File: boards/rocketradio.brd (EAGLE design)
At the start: 103.8 x 82.5 mm, 28 parts, among them T1 2N2222, X1 BU-SMA-H

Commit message: finish dumb node, update sims
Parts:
- removed C10: 0.1uF, rcl:C0603
- removed R10, R11, R12, R8, R9: (no value), rcl:R0603
- removed U$10: CSTCE16M0V53-R0, evan:MYSMD2_RESONATOR
- removed U$2, U$3: ATTINY85SOCKET, evan:SOCKET-08
- added BATT+, BATT-, COM, JP1, JP3, NC, NO: (no value), evan:1X01
- added K1: G5LE, relay:G5LE
- added MICRO, MODEM: ATTINY85SOCKET, evan:SOCKET-08
- C1: value 0.1uF -> 10uF; device rcl:C0603 -> rcl:C025-050X050
- C4, C6: value 1uF -> 0.1uF
- C5, C7: value 0.1uF -> 1uF
- R5, R6, R7: value (none) -> 400
- moved C9 250.3 mm to (48.3, 39.4), turned to 180 degrees
- moved R6 228.0 mm to (48.3, 36.8)
- moved R5 220.6 mm to (48.3, 34.3), turned to 180 degrees
- moved C1 198.5 mm to (38.1, 3.81)
- moved T1 198.4 mm to (50.8, 17.8)
- moved C8 195.9 mm to (48.3, 31.8)
- moved R7 192.6 mm to (49.5, 22.9)
- moved C3 182.1 mm to (67.3, 27.9), turned to 270 degrees
- moved C2 180.0 mm to (71.1, 27.9), turned to 270 degrees
- moved C4 160.0 mm to (3.81, 7.62), turned to 180 degrees
- moved C5 158.8 mm to (3.81, 11.4), turned to 180 degrees
- moved X1 58.5 mm to (5.08, 38.1), turned to 180 degrees
- moved R1 56.6 mm to (12.7, 6.35), turned to 90 degrees
- moved R2 51.4 mm to (16.5, 6.35), turned to 90 degrees
- moved C7 50.3 mm to (57.1, 27.9), turned to 270 degrees
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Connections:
- removed net N$17: U$10.3, U$2.2
- removed net N$18: U$10.1, U$2.3
- removed net N$8: C1.2, U$1.3
- removed net SLAVE_SELECT: R3.2, U$1.5, U$2.1, U$3.1
- removed net UART: U$2.7, U$3.7
- new net DATA_IN: MICRO.7, MODEM.2
- new net DATA_OUT: MICRO.6, MODEM.3
- new net MOD_SELECT: MICRO.1, MODEM.1, R3.2, U$1.5
- new net N$4: R5.2, U$1.3
- new net N$9: K1.S, NO.P$1
- new net TRIGGER: MICRO.5, R7.2
- net +3V3: now also BATT+.P$1, C1.1, JP1.P$1, K1.1, MICRO.8, MODEM.8; no longer R10.2, R11.2, R5.2, U$2.8, U$3.8
- net GND: now also BATT-.P$1, C1.2, C8.1, C9.1, JP3.P$1, MICRO.4, MODEM.4, T1.1; no longer C9.2, R12.1, R6.1, R8.2, R9.1, U$10.2, U$2.4, U$3.4
- net MIC_IN: now also C9.2, R6.1; no longer C8.1
- net MOD_IN: now also C8.2, MODEM.7, R5.1; no longer C10.2, R11.1, R12.2, U$2.5
- net MOD_OUT: now also MODEM.6, R6.2; no longer R7.1, U$2.6
- net N$10: now also K1.O, NC.P$1; no longer C9.1, R9.2, T1.1
- net N$11: now also COM.P$1, K1.P; no longer C10.1, R10.1, T1.3
- net N$6: now also R7.1, T1.2; no longer C8.2, R7.2, R8.1
- net N$7: now also K1.2, T1.3; no longer C1.1, R5.1, R6.2, T1.2
- net RADIO_CONTROL: now also MICRO.2; no longer U$3.2
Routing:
- net +3V3: track 0.00 -> 135.1 mm
- net MOD_SELECT: track 0.00 -> 69.8 mm, vias 0 -> 1
- net RADIO_CONTROL: track 0.00 -> 50.5 mm
- net N$4: track 0.00 -> 29.3 mm
- net TRIGGER: track 0.00 -> 28.2 mm, vias 0 -> 1
- net N$10: track 0.00 -> 21.2 mm
- net N$11: track 0.00 -> 16.2 mm
- net MIC_IN: track 0.00 -> 12.0 mm
- net N$1: track 0.00 -> 9.80 mm
- net N$7: track 0.00 -> 8.86 mm
- net N$9: track 0.00 -> 8.13 mm
- net N$6: track 0.00 -> 7.76 mm
- net MOD_IN: track 0.00 -> 6.77 mm
- net DATA_OUT: track 0.00 -> 6.35 mm
- net DATA_IN: track 0.00 -> 6.35 mm
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- added copper zone on layer 1, net GND
- added copper zone on layer 16, net GND
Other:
- board size 103.8 x 82.5 mm -> 80 x 46.7 mm
- board text added: "2016-04-13"
- board text added: "Dumb Node - V1"
- board text added: "Evan Widloski"
- board text added: "Purdue Orbital 2016"

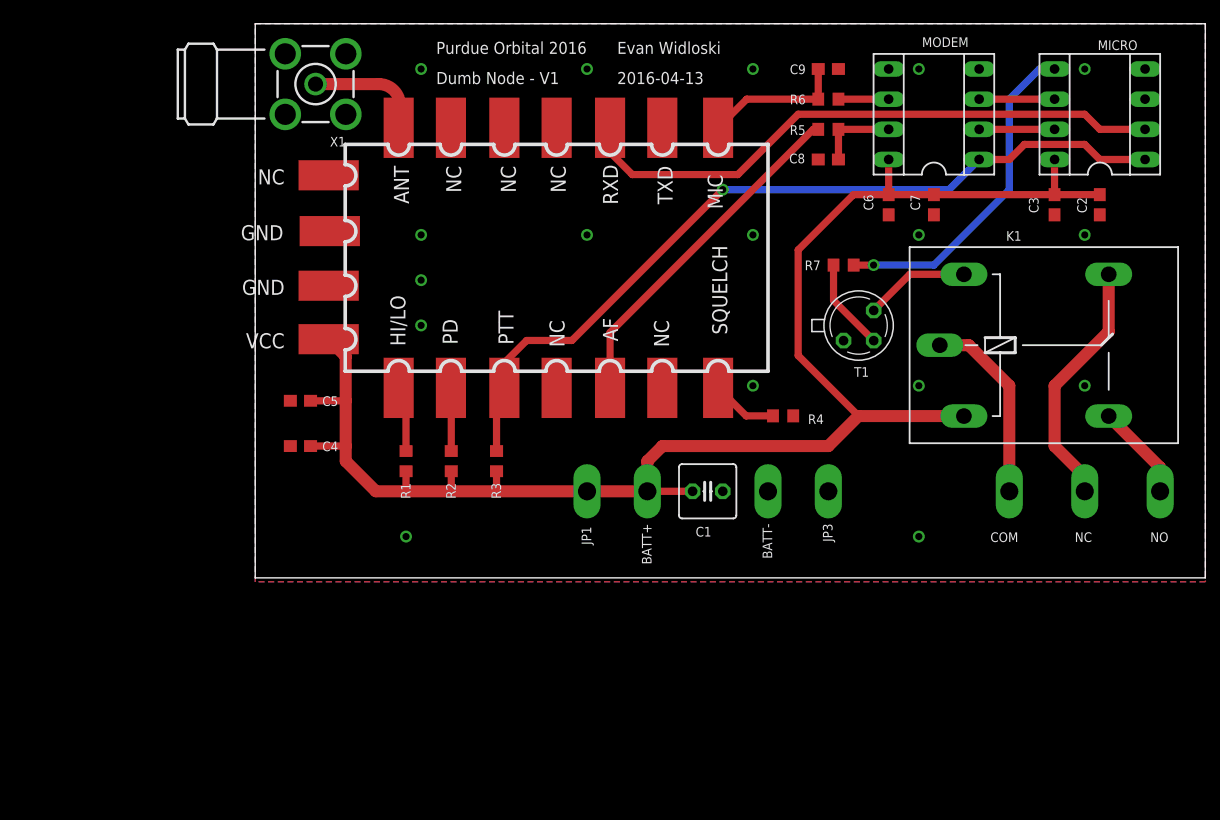
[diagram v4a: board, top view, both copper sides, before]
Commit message: use attiny84
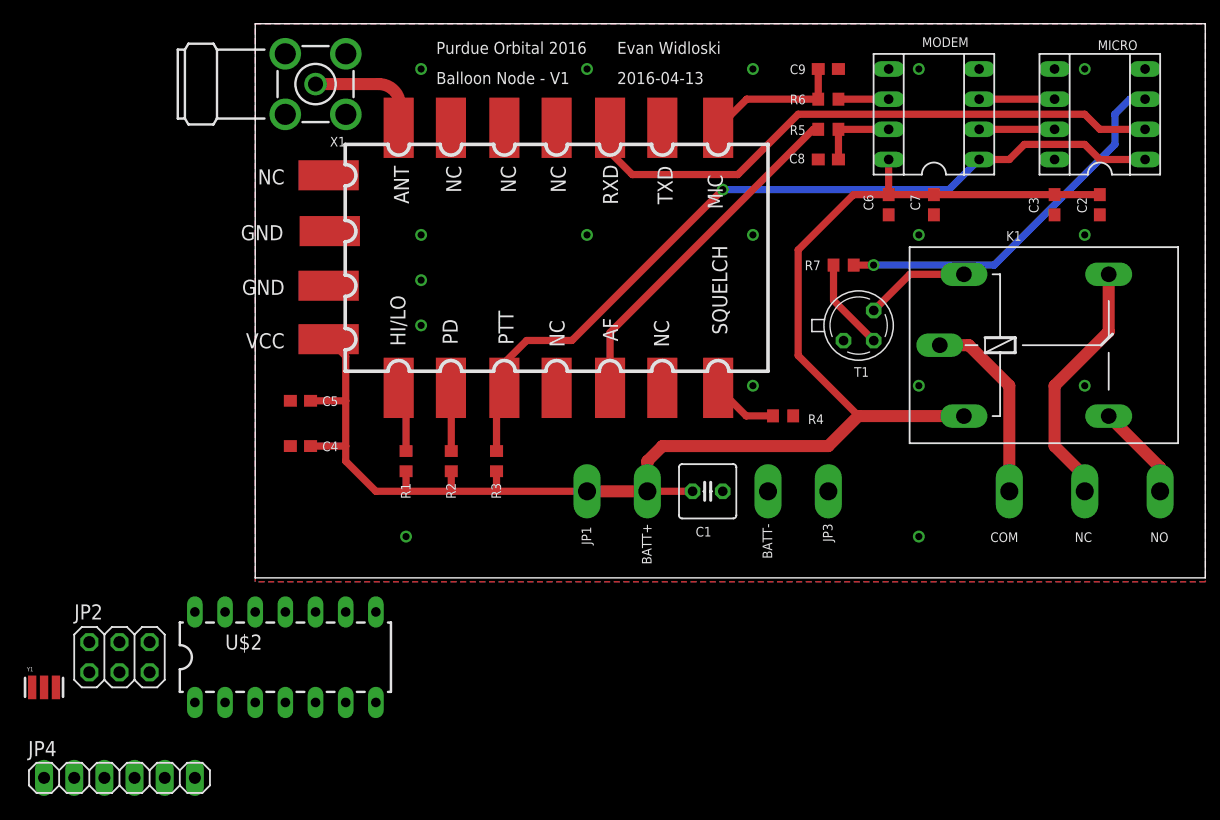
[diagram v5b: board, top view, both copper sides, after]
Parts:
- added JP2: (no value), pinhead:2X03
- added JP4: (no value), pinhead:1X06
- added U$2: ATTINY84ATTINY84-20PU, evan:DIL14
- added Y1: (no value), evan:MYSMD2_RESONATOR
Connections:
- new net MISO: JP2.1, U$2.8
- new net MOSI: JP2.4, U$2.7
- new net N$12: U$2.2, Y1.3
- new net N$8: U$2.3, Y1.1
- new net RESET: JP2.5, U$2.4
- new net SCK: JP2.3, U$2.9
- new net VCC: JP2.2
- net +3V3: now also U$2.1; no longer MICRO.8
- net DATA_IN: now also U$2.11
- net DATA_OUT: now also U$2.12
- net GND: now also JP2.6
- net MOD_SELECT: now also U$2.13
- net TRIGGER: now also MICRO.3, U$2.10; no longer MICRO.5
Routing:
- net TRIGGER: track 28.2 -> 31.8 mm
- net +3V3: track 135.1 -> 132.1 mm
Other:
- board text added: "Balloon Node - V1"
- board text removed: "Dumb Node - V1"

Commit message: update rocketradio board, complete
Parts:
- removed JP1, JP3: (no value), evan:1X01
- removed JP4: (no value), pinhead:1X06
- removed K1: G5LE, relay:G5LE
- removed R4: 10K, rcl:R0603
- removed U$1: DRA818V, dorji:DORJI
- removed U$2: ATTINY84ATTINY84-20PU, evan:DIL14
- removed X1: BU-SMA-H, con-coax:BU-SMA-H
- added 3V3: (no value), evan:1X01
- added DORJI: DRA818V, dorji:DORJI
- added ISP: (no value), pinhead:2X03
- added REG: AP1117-3.3SOT223, evan:SOT223
- added RELAY: G5LE, relay:G5LE
- added SMA: BU-SMA-H, con-coax:BU-SMA-H
- JP2: device pinhead:2X03 -> pinhead:1X04
- MICRO: value ATTINY85SOCKET -> ATTINY84ATTINY84-20PU; device evan:SOCKET-08 -> evan:DIL14
- moved Y1 106.3 mm to (78.7, 31.8), turned to 270 degrees
- moved JP2 103.6 mm to (79.2, 39.9), turned to 90 degrees
- moved R7 15.9 mm to (63.5, 30.5)
- moved COM 15.3 mm to (78.7, 5.08)
- moved T1 13.1 mm to (57.1, 29.2), turned to 270 degrees
- moved C3 12.0 mm to (78.7, 24.1), turned to 0 degrees
- moved C1 11.0 mm to (29.5, 10.7), turned to 180 degrees
- moved C7 9.25 mm to (48.3, 30.5), turned to 180 degrees
- moved BATT+ 8.98 mm to (39.4, 10.2), turned to 180 degrees
- moved NO 7.73 mm to (68.6, 5.08)
- moved C2 7.62 mm to (78.7, 27.9), turned to 0 degrees
- moved C6 7.18 mm to (48.3, 33.0), turned to 180 degrees
- moved C4 5.08 mm to (3.82, 12.7)
- moved BATT- 4.02 mm to (39.4, 2.54), turned to 180 degrees
- moved NC 4.02 mm to (73.7, 5.08)
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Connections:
- removed net MISO: JP2.1, U$2.8
- removed net MOSI: JP2.4, U$2.7
- removed net N$3: R2.2, U$1.6
- removed net N$5: R4.2, U$1.1
- removed net SCK: JP2.3, U$2.9
- new net BATT: BATT+.P$1, C1.1, REG.3
- new net PA5: DORJI.6, ISP.1, JP2.4, MICRO.8, R2.2
- new net PA6: ISP.4, JP2.3, MICRO.7
- new net PA7: JP2.2, MICRO.6
- new net PB2: JP2.1, MICRO.5
- net +3V3: now also 3V3.P$1, DORJI.8, MICRO.1, REG.2, REG.4, RELAY.1; no longer BATT+.P$1, C1.1, JP1.P$1, K1.1, R1.1, U$1.8, U$2.1
- net DATA_IN: now also MICRO.10; no longer MICRO.7, U$2.11
- net DATA_OUT: now also ISP.3, MICRO.9; no longer MICRO.6, U$2.12
- net GND: now also DORJI.10, DORJI.9, ISP.6, MICRO.14, R1.1, REG.1, SMA.2, SMA.3, SMA.4, SMA.5; no longer JP2.6, JP3.P$1, MICRO.4, R4.1, U$1.10, U$1.9, X1.2, X1.3, X1.4, X1.5
- net MIC_IN: now also DORJI.18; no longer U$1.18
- net MOD_SELECT: now also DORJI.5, MICRO.11; no longer MICRO.1, U$1.5, U$2.13
- net N$1: now also DORJI.12, SMA.1; no longer U$1.12, X1.1
- net N$10: now also RELAY.O; no longer K1.O
- net N$11: now also RELAY.P; no longer K1.P
- net N$12: now also MICRO.2; no longer U$2.2
- net N$2: now also DORJI.7; no longer U$1.7
- net N$4: now also DORJI.3; no longer U$1.3
- net N$7: now also RELAY.2; no longer K1.2
- net N$8: now also MICRO.3; no longer U$2.3
- net N$9: now also RELAY.S; no longer K1.S
- net RADIO_CONTROL: now also DORJI.16, MICRO.12; no longer MICRO.2, U$1.16
- net RESET: now also ISP.5, MICRO.4; no longer JP2.5, U$2.4
- net TRIGGER: now also MICRO.13; no longer MICRO.3, U$2.10
- net VCC: now also ISP.2; no longer JP2.2
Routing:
- net PA5: track 0.00 -> 112.9 mm, vias 0 -> 1
- net DATA_OUT: track 6.35 -> 38.1 mm
- net PA6: track 0.00 -> 29.1 mm
- net TRIGGER: track 31.8 -> 2.94 mm, vias 1 -> 0
- net RESET: track 0.00 -> 20.1 mm
- net N$11: track 16.2 -> 30.1 mm
- net BATT: track 0.00 -> 13.0 mm
- net +3V3: track 132.1 -> 143.4 mm
- net N$9: track 8.13 -> 19.1 mm
- net N$10: track 21.2 -> 12.8 mm
- net MOD_SELECT: track 69.8 -> 61.6 mm
- net N$5: track 5.60 -> 0.00 mm
- net N$3: track 5.33 -> 0.00 mm
- net PB2: track 0.00 -> 5.16 mm
- net PA7: track 0.00 -> 5.16 mm
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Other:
- board size 80 x 46.7 mm -> 85.1 x 46.9 mm
- board text added: "1"
- board text added: "B"
- board text added: "C"
- board text added: "E"
- board text added: "PA5"
- board text added: "PA6"
- board text added: "PA7"
- board text added: "PB2"
